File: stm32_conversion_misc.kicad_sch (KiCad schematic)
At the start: 49 parts, among them IC11 LM3940IMP-3.3_NOPB, J2 Micro_SD_Card, U10 W25Q16JVSS, U12 TXB0108PW, U9 TXB0108PW, Y2 Crystal_GND23

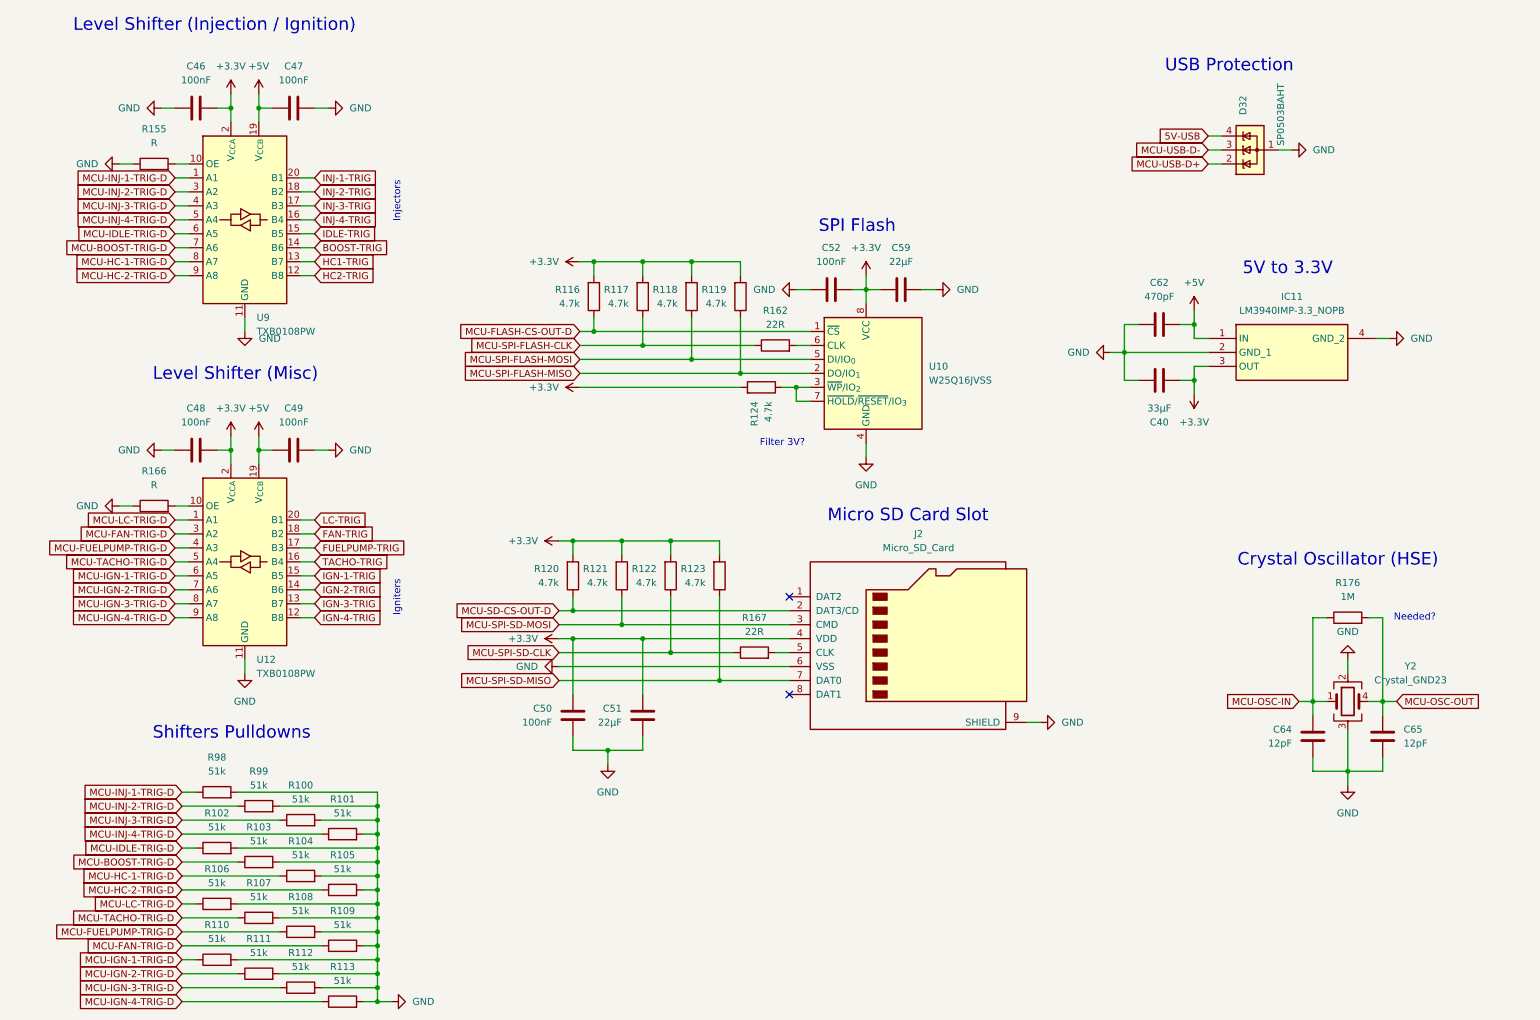
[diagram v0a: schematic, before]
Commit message: Updated reference layout
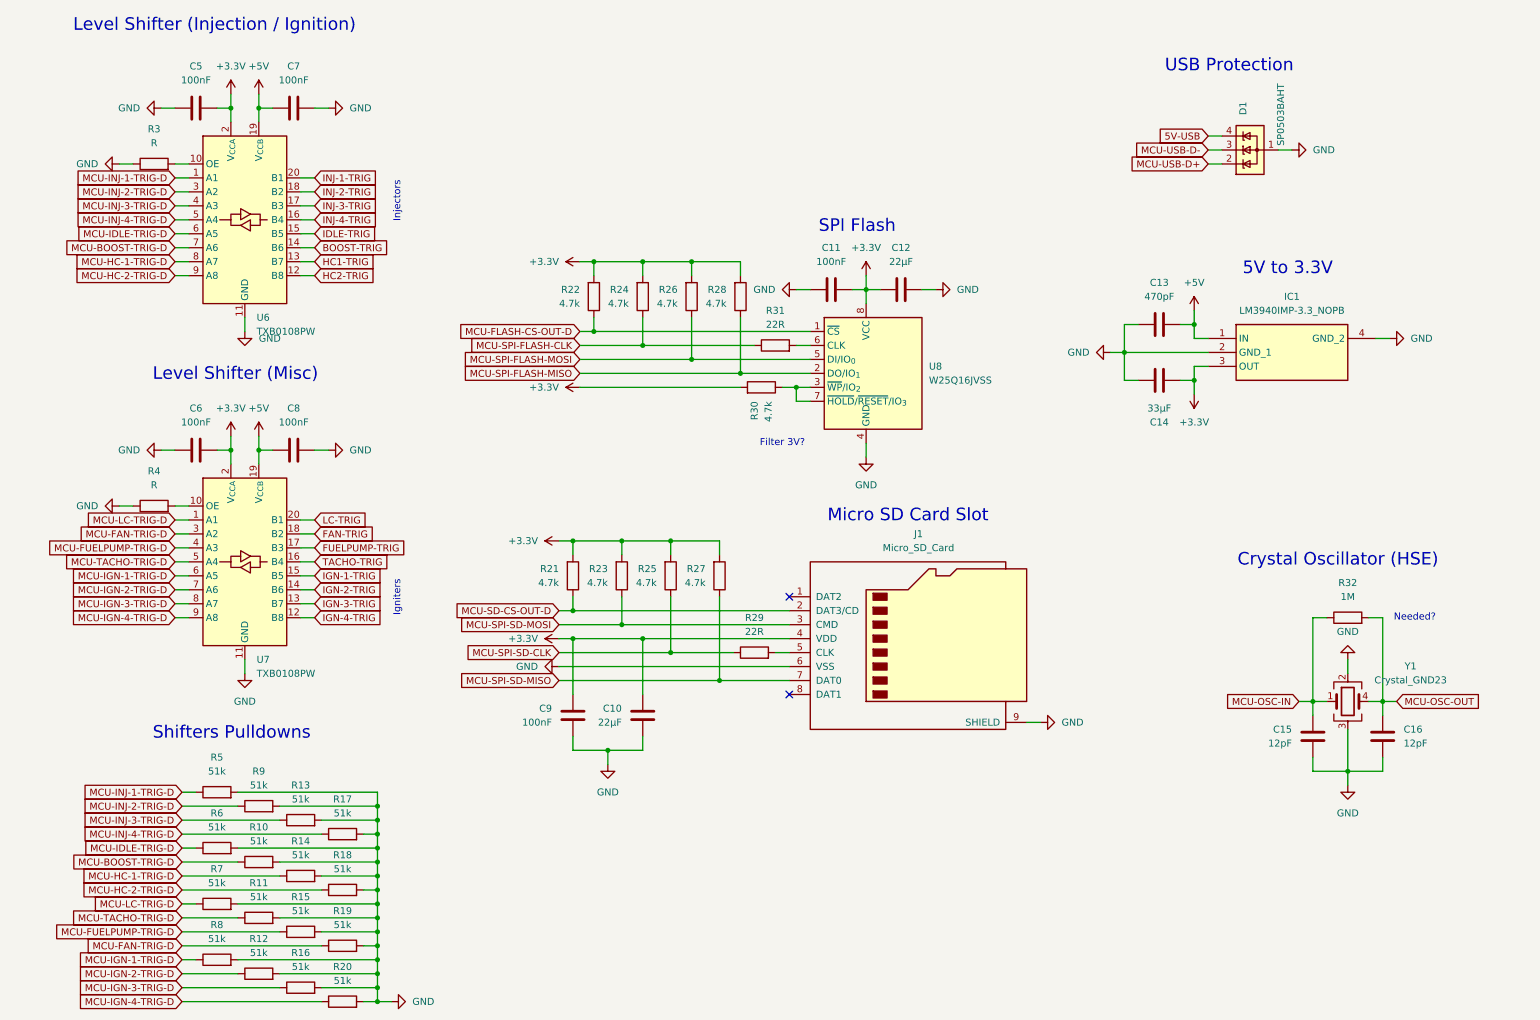
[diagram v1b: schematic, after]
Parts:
- renumbered C51 to C10, C52 to C11, C59 to C12, C62 to C13, C40 to C14, C64 to C15, C65 to C16, C46 to C5, C48 to C6, C47 to C7, C49 to C8, C50 to C9, D32 to D1, IC11 to IC1, J2 to J1, R103 to R10, R107 to R11, R111 to R12, R100 to R13, R104 to R14, R108 to R15, R112 to R16, R101 to R17, R105 to R18, R109 to R19, R113 to R20, R120 to R21, R116 to R22, R121 to R23, R117 to R24, R122 to R25, R118 to R26, R123 to R27, R119 to R28, R167 to R29, R155 to R3, R124 to R30, R162 to R31, R176 to R32, R166 to R4, R98 to R5, R102 to R6, R106 to R7, R110 to R8, R99 to R9, U9 to U6, U12 to U7, U10 to U8, Y2 to Y1

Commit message: Change power layout, add low frequency crystal
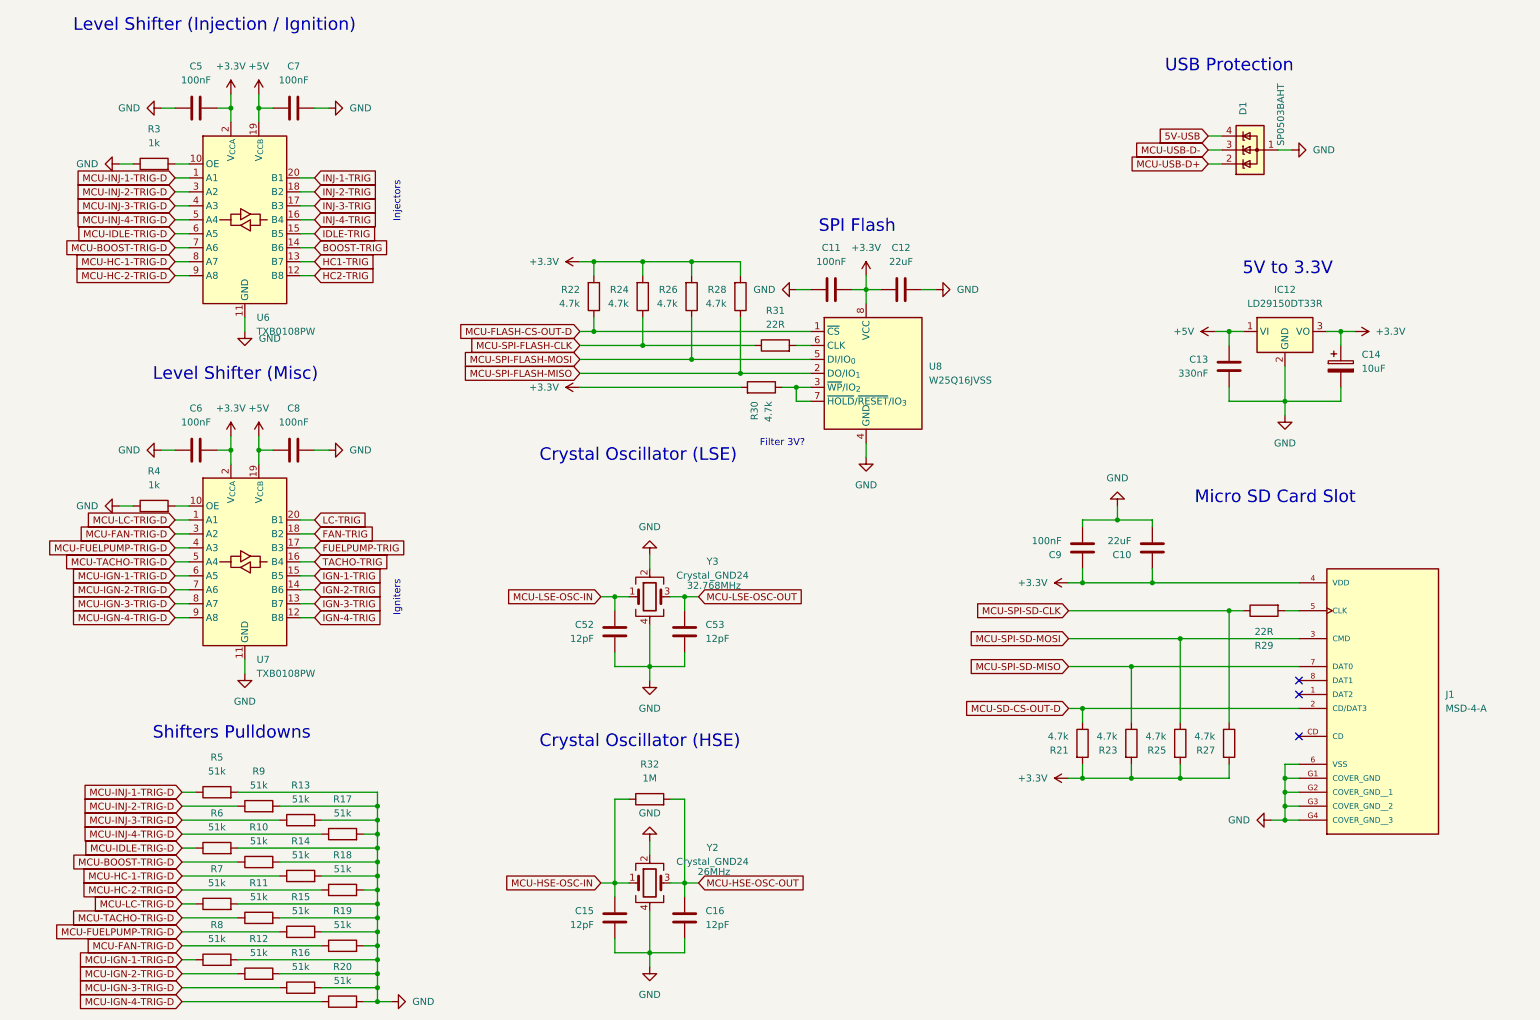
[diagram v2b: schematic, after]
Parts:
- removed C14: 33µF, Capacitor_SMD:C_0805_2012Metric, symbol Device:C
- removed IC1: LM3940IMP-3.3_NOPB, Misc:SOT230P700X180-4N, symbol Misc:LM3940IMP-3.3_NOPB
- removed J1: Micro_SD_Card, Connector_Card:microSD_HC_Molex_47219-2001, symbol Connector:Micro_SD_Card
- removed Y1: Crystal_GND23, Crystal:Crystal_SMD_5032-4Pin_5.0x3.2mm, symbol Device:Crystal_GND23
- added C14: 10uF, Capacitor_Tantalum_SMD:CP_EIA-3528-12_Kemet-T, symbol Device:C_Polarized
- added C52, C53: 12pF, Capacitor_SMD:C_0805_2012Metric, symbol Device:C
- added IC12: LD29150DT33R, Package_TO_SOT_SMD:TO-252-2, symbol Misc:LD29150DT33R
- added J1: MSD-4-A, Misc:CUI_MSD-4-A, symbol Misc:MSD-4-A
- added Y2, Y3: Crystal_GND24, Crystal:Crystal_SMD_2016-4Pin_2.0x1.6mm, symbol Device:Crystal_GND24
- C10, C12: value 22µF -> 22uF
- C13: value 470pF -> 330nF
- R3, R4: value R -> 1k
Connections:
- net +3.3V: now also C14.1, IC12.3 (VO), J1.4 (VDD)
- net +5V: now also C13.1, IC12.1 (VI); no longer C13.2
- net GND: now also C13.2, C14.2, C52.2, C53.2, IC12.2 (GND), J1.6 (VSS), J1.G1 (COVER_GND), J1.G2 (COVER_GND__1), J1.G3 (COVER_GND__2), J1.G4 (COVER_GND__3), Y2.2, Y2.4, Y3.2, Y3.4; no longer C13.1
- net MCU-SD-CS-OUT-D: now also J1.2 (CD/DAT3)
- net MCU-SPI-SD-CLK: now also R27.1; no longer R25.1
- net MCU-SPI-SD-MISO: now also R23.1, J1.7 (DAT0); no longer R27.1
- net MCU-SPI-SD-MOSI: now also R25.1, J1.3 (CMD); no longer R23.1
- net at R29.2: now also J1.5 (CLK)
- net MCU-OSC-IN renamed MCU-HSE-OSC-IN
- net MCU-HSE-OSC-IN: now also Y2.1
- net MCU-OSC-OUT renamed MCU-HSE-OSC-OUT
- net MCU-HSE-OSC-OUT: now also Y2.3
- new net MCU-LSE-OSC-IN: C52.1, Y3.1
- new net MCU-LSE-OSC-OUT: C53.1, Y3.3
- no-connect marks 2 -> 3
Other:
- note added: "Crystal Oscillator (LSE)"
- note removed: "Needed?"
- moved on the sheet: C10, C15, C16, C9, R21, R23, R25, R27, R29, R32
